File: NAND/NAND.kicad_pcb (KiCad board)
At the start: 2 copper layers, 7.9 x 20.6 mm, 7 parts, among them J1 5-146280-3-ND, J2 5-146280-3-ND, Q1 DMP2004K-7, Q2 DMP2004K-7

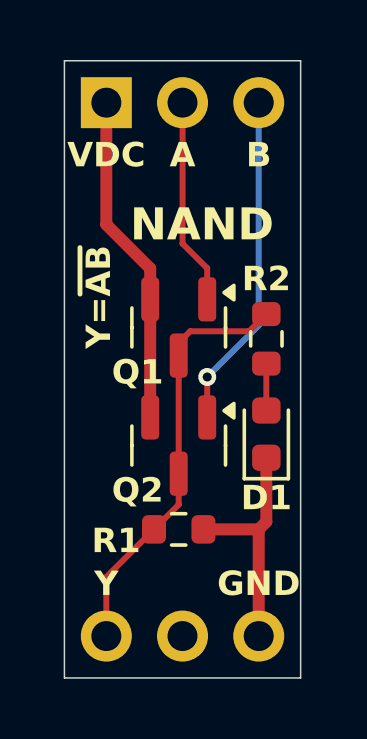
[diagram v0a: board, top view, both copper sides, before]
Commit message: Finish NOR gate PCB and unify NAND with it
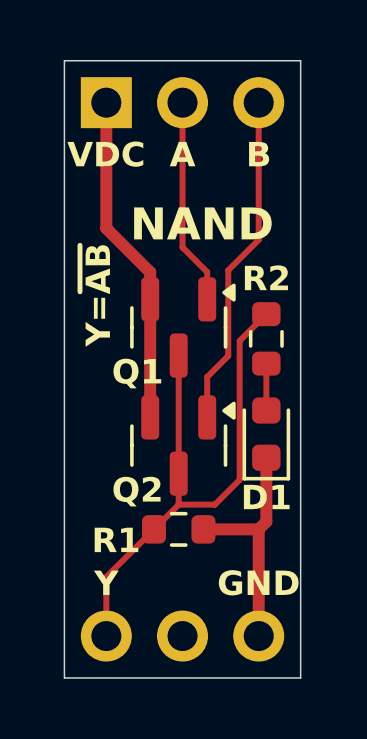
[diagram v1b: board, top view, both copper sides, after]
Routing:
- net /Y: track 14.1 -> 18.6 mm
- net /B: vias 1 -> 0
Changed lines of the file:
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@@
 	)
 	(gr_text "Y=~{AB}"
-		(at 126.746 82.677 90)
-		(layer "F.SilkS")
-		(effects
-			(font
-				(size 0.8128 0.8128)
-				(thickness 0.16256)
-				(bold yes)
-			)
+		(at 126.746 84.328 90)
+		(layer "F.SilkS")
+		(effects
+			(font
+				(size 0.8128 0.8128)
+				(thickness 0.16256)
+				(bold yes)
+			)
+			(justify left)
 		)
 	)
@@
 	)
 	(segment
-		(start 131.763 83.82)
-		(end 129.794 83.82)
-		(width 0.2)
-		(layer "F.Cu")
-		(net 3)
-	)
-	(segment
 		(start 129.413 88.5675)
 		(end 129.413 84.6305)
@@
 	)
 	(segment
-		(start 129.794 83.82)
-		(end 129.413 84.201)
-		(width 0.2)
-		(layer "F.Cu")
-		(net 3)
-	)
-	(segment
-		(start 129.413 84.201)
-		(end 129.413 84.6305)
-		(width 0.2)
-		(layer "F.Cu")
-		(net 3)
-	)
-	(segment
 		(start 129.413 89.599)
 		(end 128.588 90.424)
@@
 	)
 	(segment
+		(start 130.619 89.599)
+		(end 131.445 88.773)
+		(width 0.2)
+		(layer "F.Cu")
+		(net 3)
+	)
+	(segment
+		(start 131.445 88.773)
+		(end 131.445 84.138)
+		(width 0.2)
+		(layer "F.Cu")
+		(net 3)
+	)
+	(segment
+		(start 129.413 89.599)
+		(end 130.619 89.599)
+		(width 0.2)
+		(layer "F.Cu")
+		(net 3)
+	)
+	(segment
+		(start 131.445 84.138)
+		(end 132.334 83.249)
+		(width 0.2)
+		(layer "F.Cu")
+		(net 3)
+	)
+	(segment
 		(start 129.413 88.5675)
 		(end 129.413 89.599)
@@
 	)
 	(segment
-		(start 132.334 83.249)
-		(end 131.763 83.82)
-		(width 0.2)
-		(layer "F.Cu")
-		(net 3)
-	)
-	(segment
-		(start 128.463 82.7555)
-		(end 128.463 81.727)
-		(width 0.4)
-		(layer "F.Cu")
-		(net 4)
-	)
-	(segment
-		(start 128.463 81.727)
-		(end 127 80.264)
+		(start 128.463 81.854)
+		(end 127 80.391)
+		(width 0.4)
+		(layer "F.Cu")
+		(net 4)
+	)
+	(segment
+		(start 127 80.391)
+		(end 127 76.2)
 		(width 0.4)
 		(layer "F.Cu")
@@
 	)
 	(segment
-		(start 127 80.264)
-		(end 127 76.2)
-		(width 0.4)
-		(layer "F.Cu")
-		(net 4)
+		(start 128.463 82.7555)
+		(end 128.463 81.854)
+		(width 0.4)
+		(layer "F.Cu")
+		(net 4)
+	)
+	(segment
+		(start 132.08 80.772)
+		(end 132.08 76.2)
+		(width 0.2)
+		(layer "F.Cu")
+		(net 5)
+	)
+	(segment
+		(start 130.363 85.344)
+		(end 131.064 84.643)
+		(width 0.2)
+		(layer "F.Cu")
+		(net 5)
+	)
+	(segment
+		(start 131.064 84.643)
+		(end 131.064 81.788)
+		(width 0.2)
+		(layer "F.Cu")
+		(net 5)
 	)
 	(segment
@@
 		(net 5)
 	)
-	(via
-		(at 130.363 85.344)
-		(size 0.6)
-		(drill 0.3)
-		(layers "F.Cu" "B.Cu")
-		(net 5)
-	)
-	(segment
-		(start 132.08 76.2)
-		(end 132.08 83.627)
-		(width 0.2)
-		(layer "B.Cu")
-		(net 5)
-	)
-	(segment
-		(start 132.08 83.627)
-		(end 130.363 85.344)
-		(width 0.2)
-		(layer "B.Cu")
-		(net 5)
-	)
-	(segment
-		(start 130.363 81.722)
-		(end 129.54 80.899)
+	(segment
+		(start 131.064 81.788)
+		(end 132.08 80.772)
+		(width 0.2)
+		(layer "F.Cu")
+		(net 5)
+	)
+	(segment
+		(start 130.363 81.849)
+		(end 129.54 81.026)
 		(width 0.2)
 		(layer "F.Cu")
@@
 	)
 	(segment
+		(start 129.54 81.026)
+		(end 129.54 76.2)
+		(width 0.2)
+		(layer "F.Cu")
+		(net 6)
+	)
+	(segment
 		(start 130.363 82.7555)
-		(end 130.363 81.722)
-		(width 0.2)
-		(layer "F.Cu")
-		(net 6)
-	)
-	(segment
-		(start 129.54 80.899)
-		(end 129.54 76.2)
-		(width 0.2)
-		(layer "F.Cu")
+		(end 130.363 81.849)
+		(width 0.2)
+		(layer "F.Cu")

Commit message: Change pull-down resistor to 0.1w
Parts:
- D1: value LED -> Green
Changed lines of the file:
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@@
 			)
 		)
-		(property "Value" "LED"
+		(property "Value" "Green"
 			(at 0 1.43 90)
 			(layer "F.Fab")
@@
 			)
 		)
-		(property "Datasheet" "https://fscdn.rohm.com/en/products/databook/datasheet/passive/resistor/chip_resistor/esr-e.pdf"
+		(property "Datasheet" "https://www.yageo.com/upload/media/product/products/datasheet/rchip/PYu-RC_Group_51_RoHS_L_12.pdf"
 			(at 0 0 0)
 			(unlocked yes)
@@
 			)
 		)
-		(property "Description" "10 kOhms ±5% 0.25W, 1/4W Chip Resistor 0603 (1608 Metric)"
+		(property "Description" "10 kOhms ±1% 0.1W, 1/10W Chip Resistor 0603"
 			(at 0 0 0)
 			(unlocked yes)
